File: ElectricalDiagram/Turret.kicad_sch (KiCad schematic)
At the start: 29 parts, among them J1 Conn_01x02_Pin, J1 Conn_01x04_Pin, J2 Conn_01x02_Pin

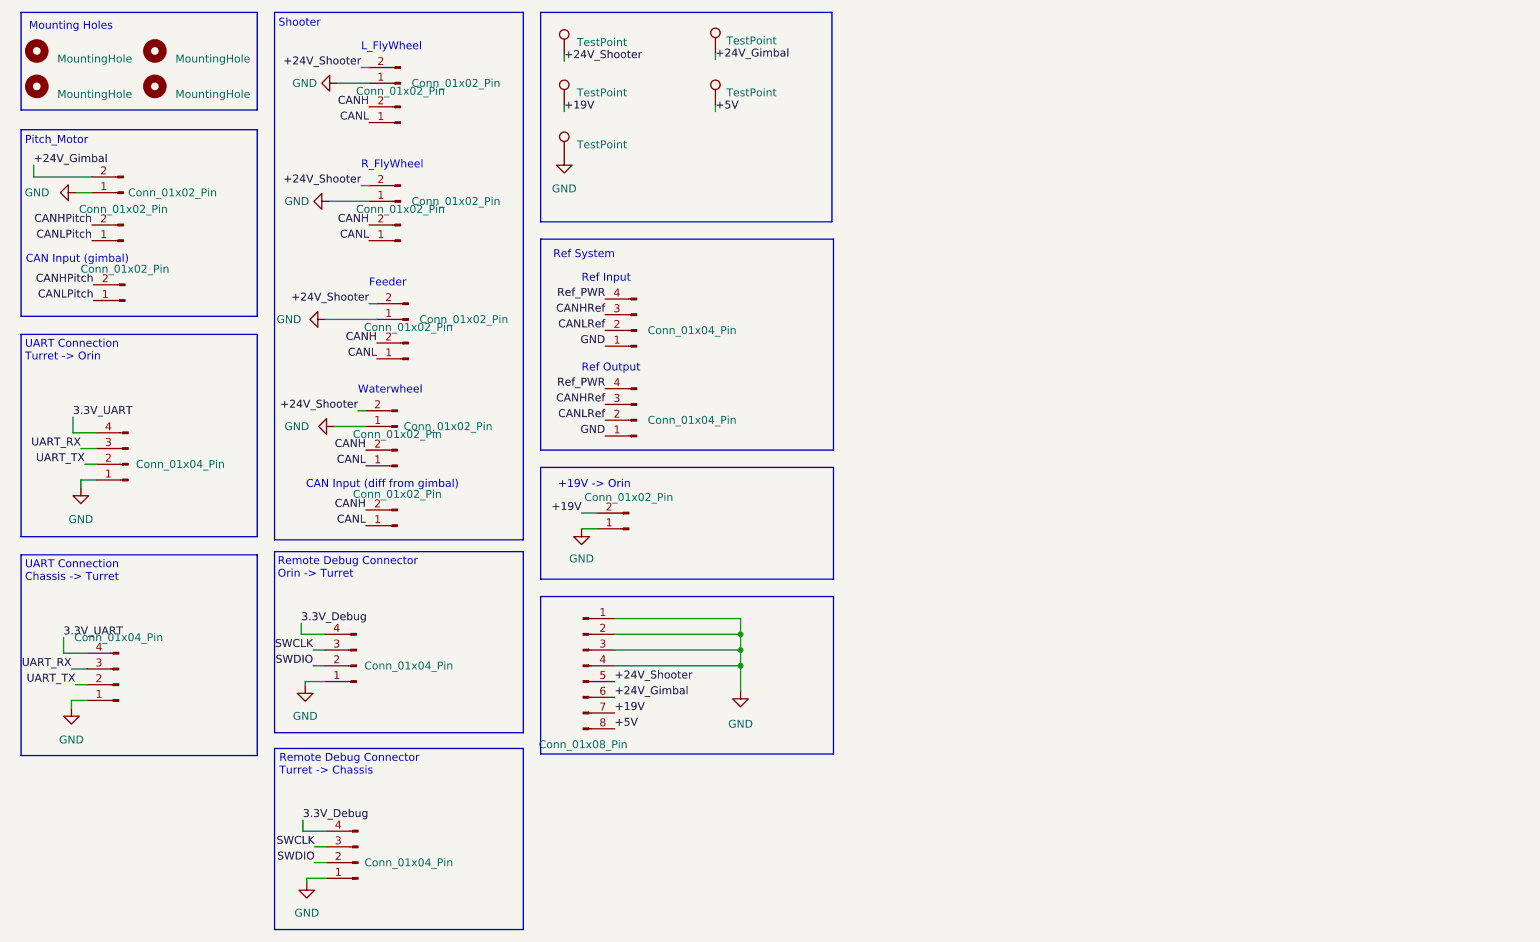
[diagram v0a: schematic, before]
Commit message: Updated electrical diagram and Kicad library
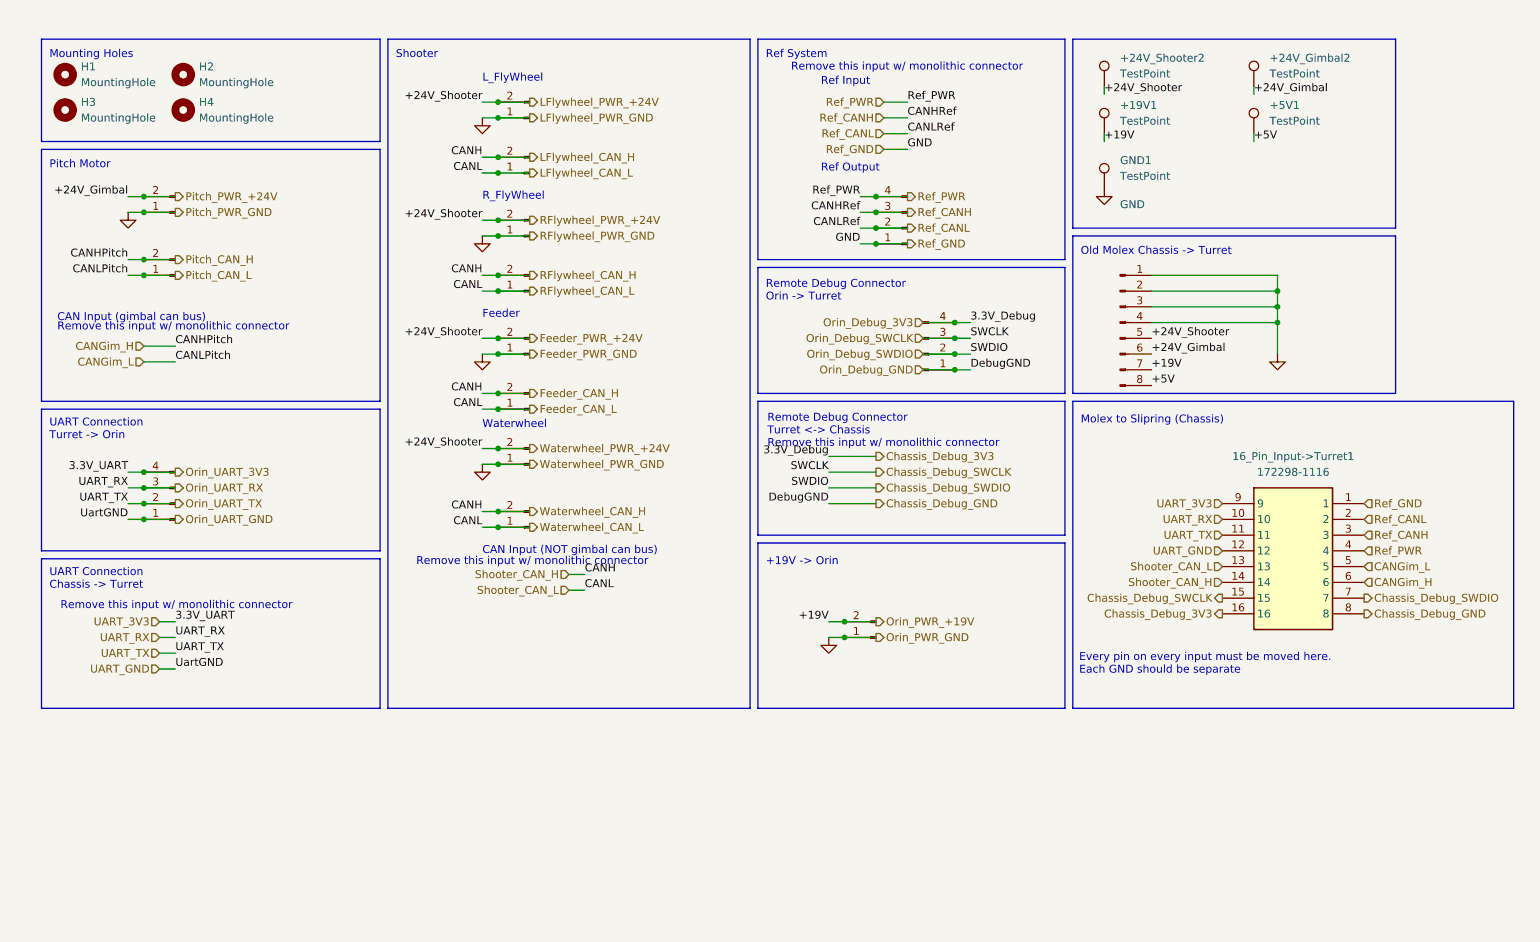
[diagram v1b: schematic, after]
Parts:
- removed J1 (x6), J2, J? (x6): Conn_01x02_Pin, symbol Connector:Conn_01x02_Pin
- removed J1 (x6): Conn_01x04_Pin, symbol Connector:Conn_01x04_Pin
- removed J?: Conn_01x08_Pin, symbol Connector:Conn_01x08_Pin
- removed TP1, TP? (x4): TestPoint, symbol Connector:TestPoint
- added +19V1, +24V_Gimbal2, +24V_Shooter2, +5V1, GND1: TestPoint, TestPoint:TestPoint_Loop_D1.80mm_Drill1.0mm_Beaded, symbol Connector:TestPoint
- added +19V_Turret->Orin1, +24V_Feeder1, +24V_Gimbal1, +24V_L_Flywheel1, +24V_R_Flywheel1, +24V_Waterwheel1: Conn_01x02_Pin, Connector_AMASS:AMASS_XT30U-F_1x02_P5.0mm_Vertical, symbol Connector:Conn_01x02_Pin
- added 16_Pin_Input->Turret1: 172298-1116, Connectors:172298-YY16, symbol Robomaster_Library:172298-1116
- added 8_Pin_Slipring->Turret1: Conn_01x08_Pin, Connectors:CON_1722981108_MOL, symbol Connector:Conn_01x08_Pin
- added CAN_Feeder1, CAN_Gimbal1, CAN_L_Flywheel1, CAN_R_Flywheel1, CAN_Waterwheel1: Conn_01x02_Pin, Connector_JST:JST_GH_BM02B-GHS-TBT_1x02-1MP_P1.25mm_Vertical, symbol Connector:Conn_01x02_Pin
- added Debug_Orin->Turret1, Ref_Out1, UART_Turret->Orin1: Conn_01x04_Pin, Connector_JST:JST_GH_BM04B-GHS-TBT_1x04-1MP_P1.25mm_Vertical, symbol Connector:Conn_01x04_Pin
- H1, H2, H3, H4: footprint (none) -> MountingHole:MountingHole_3mm; now in the parts list
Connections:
- net +5V: now also +5V1.1, 8_Pin_Slipring->Turret1.8 (Pin_8)
- net GND: now also +19V_Turret->Orin1.1 (Pin_1), +24V_Feeder1.1 (Pin_1), +24V_Gimbal1.1 (Pin_1), +24V_L_Flywheel1.1 (Pin_1), +24V_R_Flywheel1.1 (Pin_1), +24V_Waterwheel1.1 (Pin_1), 16_Pin_Input->Turret1.1, 8_Pin_Slipring->Turret1.1 (Pin_1), 8_Pin_Slipring->Turret1.2 (Pin_2), 8_Pin_Slipring->Turret1.3 (Pin_3), 8_Pin_Slipring->Turret1.4 (Pin_4), GND1.1, Ref_Out1.1 (Pin_1)
- net Ref_PWR: now also 16_Pin_Input->Turret1.4, Ref_Out1.4 (Pin_4)
- new net CANGim_H: 16_Pin_Input->Turret1.6, CAN_Gimbal1.2 (Pin_2)
- new net CANGim_L: 16_Pin_Input->Turret1.5, CAN_Gimbal1.1 (Pin_1)
- new net Chassis_Debug_3V3: 16_Pin_Input->Turret1.16, Debug_Orin->Turret1.4 (Pin_4)
- new net Chassis_Debug_GND: 16_Pin_Input->Turret1.8, Debug_Orin->Turret1.1 (Pin_1)
- new net Chassis_Debug_SWCLK: 16_Pin_Input->Turret1.15, Debug_Orin->Turret1.3 (Pin_3)
- new net Chassis_Debug_SWDIO: 16_Pin_Input->Turret1.7, Debug_Orin->Turret1.2 (Pin_2)
- new net Feeder_CAN_H: 16_Pin_Input->Turret1.14, CAN_Feeder1.2 (Pin_2), CAN_L_Flywheel1.2 (Pin_2), CAN_R_Flywheel1.2 (Pin_2), CAN_Waterwheel1.2 (Pin_2)
- new net Feeder_CAN_L: 16_Pin_Input->Turret1.13, CAN_Feeder1.1 (Pin_1), CAN_L_Flywheel1.1 (Pin_1), CAN_R_Flywheel1.1 (Pin_1), CAN_Waterwheel1.1 (Pin_1)
- new net Feeder_PWR_+24V: +24V_Feeder1.2 (Pin_2), +24V_L_Flywheel1.2 (Pin_2), +24V_R_Flywheel1.2 (Pin_2), +24V_Shooter2.1, +24V_Waterwheel1.2 (Pin_2), 8_Pin_Slipring->Turret1.5 (Pin_5)
- new net Orin_PWR_+19V: +19V1.1, +19V_Turret->Orin1.2 (Pin_2), 8_Pin_Slipring->Turret1.7 (Pin_7)
- new net Orin_UART_3V3: 16_Pin_Input->Turret1.9, UART_Turret->Orin1.4 (Pin_4)
- new net Orin_UART_GND: 16_Pin_Input->Turret1.12, UART_Turret->Orin1.1 (Pin_1)
- new net Orin_UART_RX: 16_Pin_Input->Turret1.10, UART_Turret->Orin1.3 (Pin_3)
- new net Orin_UART_TX: 16_Pin_Input->Turret1.11, UART_Turret->Orin1.2 (Pin_2)
- new net Pitch_PWR_+24V: +24V_Gimbal1.2 (Pin_2), +24V_Gimbal2.1, 8_Pin_Slipring->Turret1.6 (Pin_6)
- new net Ref_CANH: 16_Pin_Input->Turret1.3, Ref_Out1.3 (Pin_3)
- new net Ref_CANL: 16_Pin_Input->Turret1.2, Ref_Out1.2 (Pin_2)
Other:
- note added: "CAN Input (NOT gimbal can bus)"
- note added: "CAN Input (gimbal can bus)"
- note added: "Every pin on every input must be moved here. Each GND should be separate"
- note added: "Molex to Slipring (Chassis)"
- note added: "Old Molex Chassis -> Turret"
- note added: "Pitch Motor"
- note added: "Remote Debug Connector Turret <-> Chassis"
- note added: "Remove this input w/ monolithic connector"
- note removed: "CAN Input (diff from gimbal)"
- note removed: "CAN Input (gimbal)"
- note removed: "Pitch_Motor"
- note removed: "Remote Debug Connector Turret -> Chassis"
